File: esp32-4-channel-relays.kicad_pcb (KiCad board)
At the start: 2 copper layers, 86.4 x 86.6 mm, 63 parts, among them J1 Relay-1, J2 Relay-2, J3 Relay-3, J4 Relay-4, K1 SRD-05VDC-SL-C, K2 SRD-05VDC-SL-C, K3 SRD-05VDC-SL-C, K4 SRD-05VDC-SL-C, Q1 MBT3904DW1, Q2 BC547A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

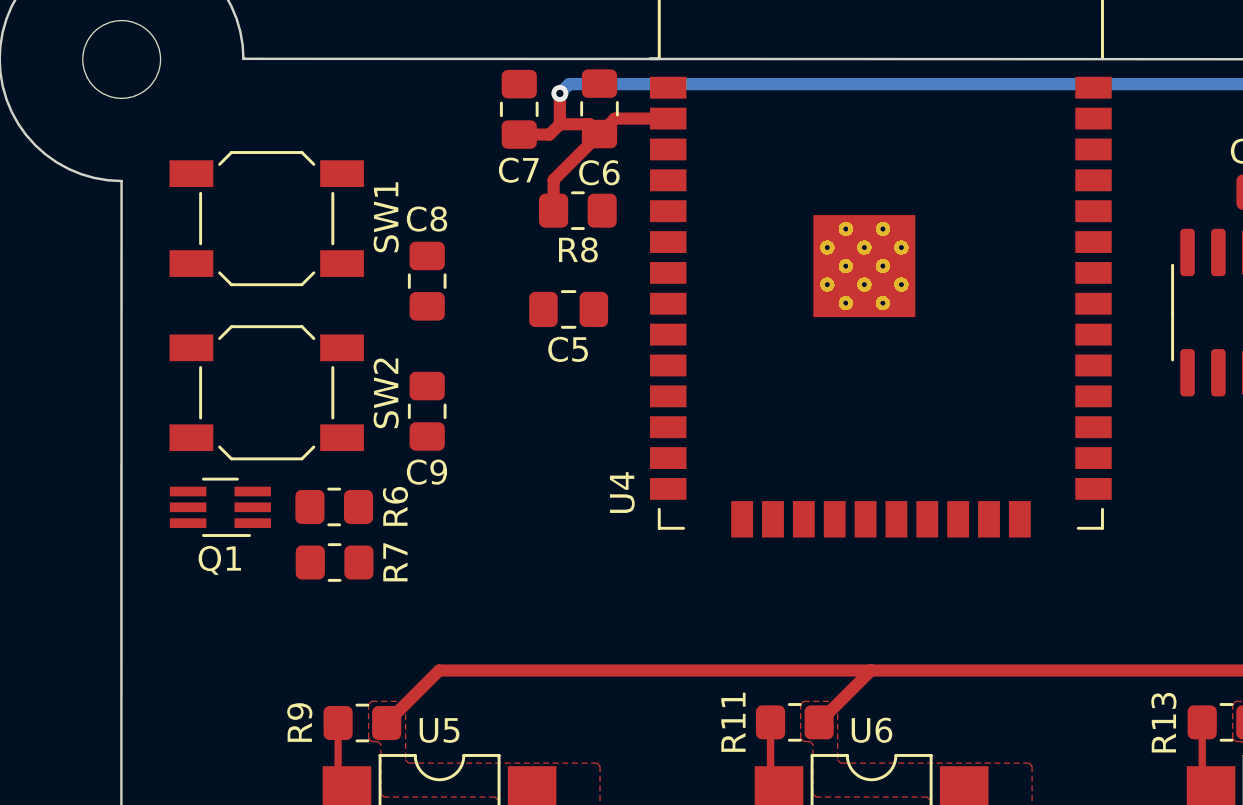
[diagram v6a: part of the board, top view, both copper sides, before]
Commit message: Routing Reset, Reset switch button and IO_0, IO_0 switch button
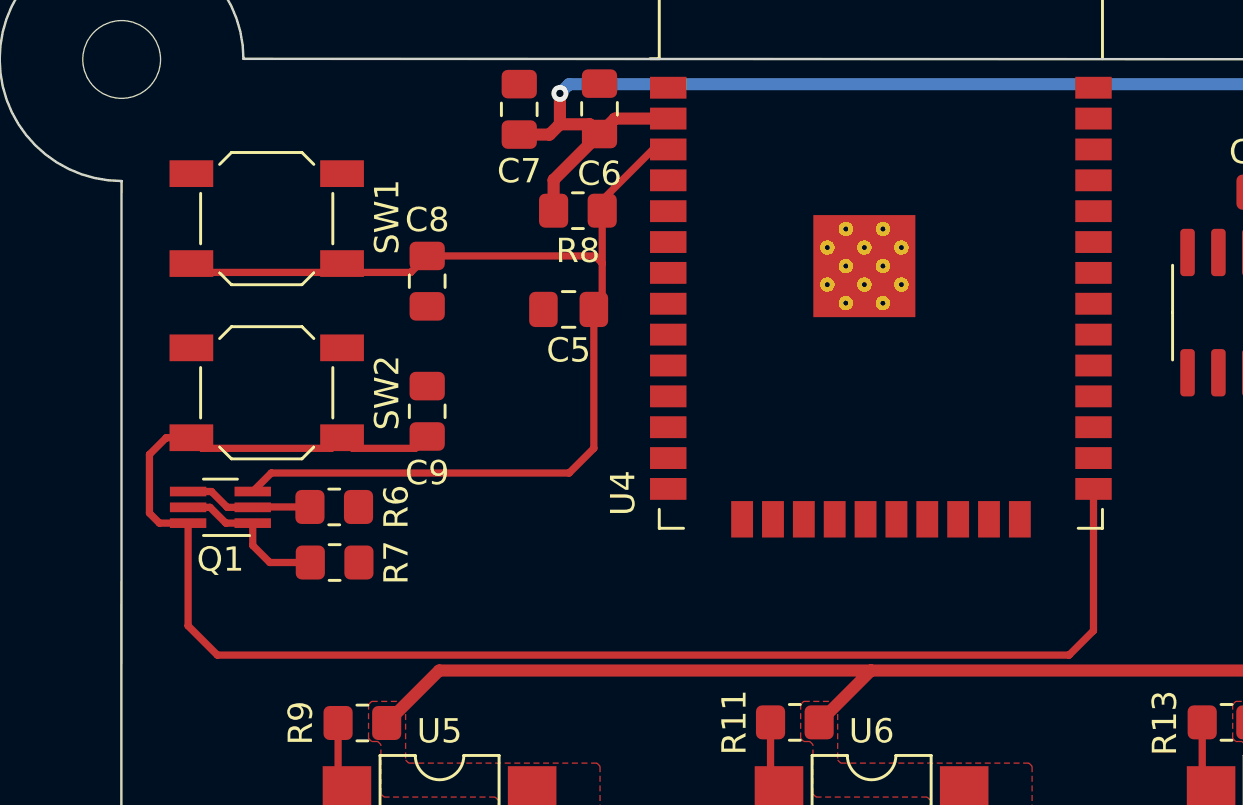
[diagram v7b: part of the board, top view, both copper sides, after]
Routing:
- net /IO_0: track 0.00 -> 64.9 mm
- net /RESET: track 0.00 -> 46.5 mm
- net Net-(Q1-B2): track 0.00 -> 6.51 mm
- net Net-(Q1-B1): track 0.00 -> 5.29 mm
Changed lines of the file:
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@@
   (segment (start 173.99 54.61) (end 145.034 54.61) (width 0.5) (layer "B.Cu") (net 3))
   (segment (start 175.387 57.531) (end 175.387 56.007) (width 0.5) (layer "B.Cu") (net 3))
+  (segment (start 129.488 61.993) (end 129.852 62.357) (width 0.3) (layer "F.Cu") (net 4))
+  (segment (start 135.688 61.993) (end 136.052 62.357) (width 0.3) (layer "F.Cu") (net 4))
+  (segment (start 146.3935 59.817) (end 146.3935 61.976) (width 0.3) (layer "F.Cu") (net 4))
+  (segment (start 132.775 70.612) (end 145.034 70.612) (width 0.3) (layer "F.Cu") (net 4))
+  (segment (start 146.0965 61.679) (end 146.3935 61.976) (width 0.3) (layer "F.Cu") (net 4))
+  (segment (start 146.3935 59.3845) (end 146.3935 59.817) (width 0.3) (layer "F.Cu") (net 4))
+  (segment (start 139.192 61.679) (end 146.0965 61.679) (width 0.3) (layer "F.Cu") (net 4))
+  (segment (start 132.013 71.374) (end 132.775 70.612) (width 0.3) (layer "F.Cu") (net 4))
+  (segment (start 148.481 57.297) (end 146.3935 59.3845) (width 0.3) (layer "F.Cu") (net 4))
+  (segment (start 146.05 69.596) (end 146.05 63.881) (width 0.3) (layer "F.Cu") (net 4))
+  (segment (start 136.052 62.357) (end 138.514 62.357) (width 0.3) (layer "F.Cu") (net 4))
+  (segment (start 129.852 62.357) (end 135.324 62.357) (width 0.3) (layer "F.Cu") (net 4))
+  (segment (start 145.034 70.612) (end 146.05 69.596) (width 0.3) (layer "F.Cu") (net 4))
+  (segment (start 146.3935 63.5375) (end 146.05 63.881) (width 0.3) (layer "F.Cu") (net 4))
+  (segment (start 146.3935 61.976) (end 146.3935 63.5375) (width 0.3) (layer "F.Cu") (net 4))
+  (segment (start 138.514 62.357) (end 139.192 61.679) (width 0.3) (layer "F.Cu") (net 4))
+  (segment (start 149.111 57.297) (end 148.481 57.297) (width 0.3) (layer "F.Cu") (net 4))
+  (segment (start 135.324 62.357) (end 135.688 61.993) (width 0.3) (layer "F.Cu") (net 4))
+  (segment (start 129.924 69.596) (end 135.252 69.596) (width 0.3) (layer "F.Cu") (net 5))
+  (segment (start 166.611 77.102) (end 166.611 71.267) (width 0.3) (layer "F.Cu") (net 5))
+  (segment (start 136.124 69.596) (end 138.7055 69.596) (width 0.3) (layer "F.Cu") (net 5))
+  (segment (start 128.452 69.16) (end 129.488 69.16) (width 0.3) (layer "F.Cu") (net 5))
+  (segment (start 129.353 76.902) (end 130.556 78.105) (width 0.3) (layer "F.Cu") (net 5))
+  (segment (start 127.762 69.85) (end 128.452 69.16) (width 0.3) (layer "F.Cu") (net 5))
+  (segment (start 135.252 69.596) (end 135.688 69.16) (width 0.3) (layer "F.Cu") (net 5))
+  (segment (start 129.353 72.674) (end 129.353 76.902) (width 0.3) (layer "F.Cu") (net 5))
+  (segment (start 130.556 78.105) (end 165.608 78.105) (width 0.3) (layer "F.Cu") (net 5))
+  (segment (start 127.762 72.263) (end 127.762 69.85) (width 0.3) (layer "F.Cu") (net 5))
+  (segment (start 135.688 69.16) (end 136.124 69.596) (width 0.3) (layer "F.Cu") (net 5))
+  (segment (start 129.353 72.674) (end 128.173 72.674) (width 0.3) (layer "F.Cu") (net 5))
+  (segment (start 129.488 69.16) (end 129.924 69.596) (width 0.3) (layer "F.Cu") (net 5))
+  (segment (start 138.7055 69.596) (end 139.192 69.1095) (width 0.3) (layer "F.Cu") (net 5))
+  (segment (start 165.608 78.105) (end 166.611 77.102) (width 0.3) (layer "F.Cu") (net 5))
+  (segment (start 128.173 72.674) (end 127.762 72.263) (width 0.3) (layer "F.Cu") (net 5))
   (segment (start 192.897 73.406) (end 195.063 73.406) (width 0.3) (layer "F.Cu") (net 6))
   (segment (start 135.89 86.106) (end 135.89 87.376) (width 0.3) (layer "F.Cu") (net 8))
@@
   (segment (start 191.516 66.421) (end 190.754 65.659) (width 0.5) (layer "B.Cu") (net 19))
   (segment (start 194.056 66.294) (end 194.183 66.421) (width 0.5) (layer "B.Cu") (net 19))
+  (segment (start 132.715 74.295) (end 132.013 73.593) (width 0.3) (layer "F.Cu") (net 32))
+  (segment (start 130.905894 72.674) (end 132.013 72.674) (width 0.3) (layer "F.Cu") (net 32))
+  (segment (start 132.013 73.593) (end 132.013 72.674) (width 0.3) (layer "F.Cu") (net 32))
+  (segment (start 130.255894 72.024) (end 130.905894 72.674) (width 0.3) (layer "F.Cu") (net 32))
+  (segment (start 129.353 72.024) (end 130.255894 72.024) (width 0.3) (layer "F.Cu") (net 32))
+  (segment (start 134.382 74.295) (end 132.715 74.295) (width 0.3) (layer "F.Cu") (net 32))
+  (segment (start 132.028 72.009) (end 132.013 72.024) (width 0.3) (layer "F.Cu") (net 33))
+  (segment (start 132.013 72.024) (end 130.963 72.024) (width 0.3) (layer "F.Cu") (net 33))
+  (segment (start 130.313 71.374) (end 129.353 71.374) (width 0.3) (layer "F.Cu") (net 33))
+  (segment (start 134.366 72.009) (end 132.028 72.009) (width 0.3) (layer "F.Cu") (net 33))
+  (segment (start 130.963 72.024) (end 130.313 71.374) (width 0.3) (layer "F.Cu") (net 33))
   (segment (start 133.736 90.424) (end 139.335 90.424) (width 0.3) (layer "F.Cu") (net 34))
   (segment (start 132.715 91.445) (end 133.736 90.424) (width 0.3) (layer "F.Cu") (net 34))

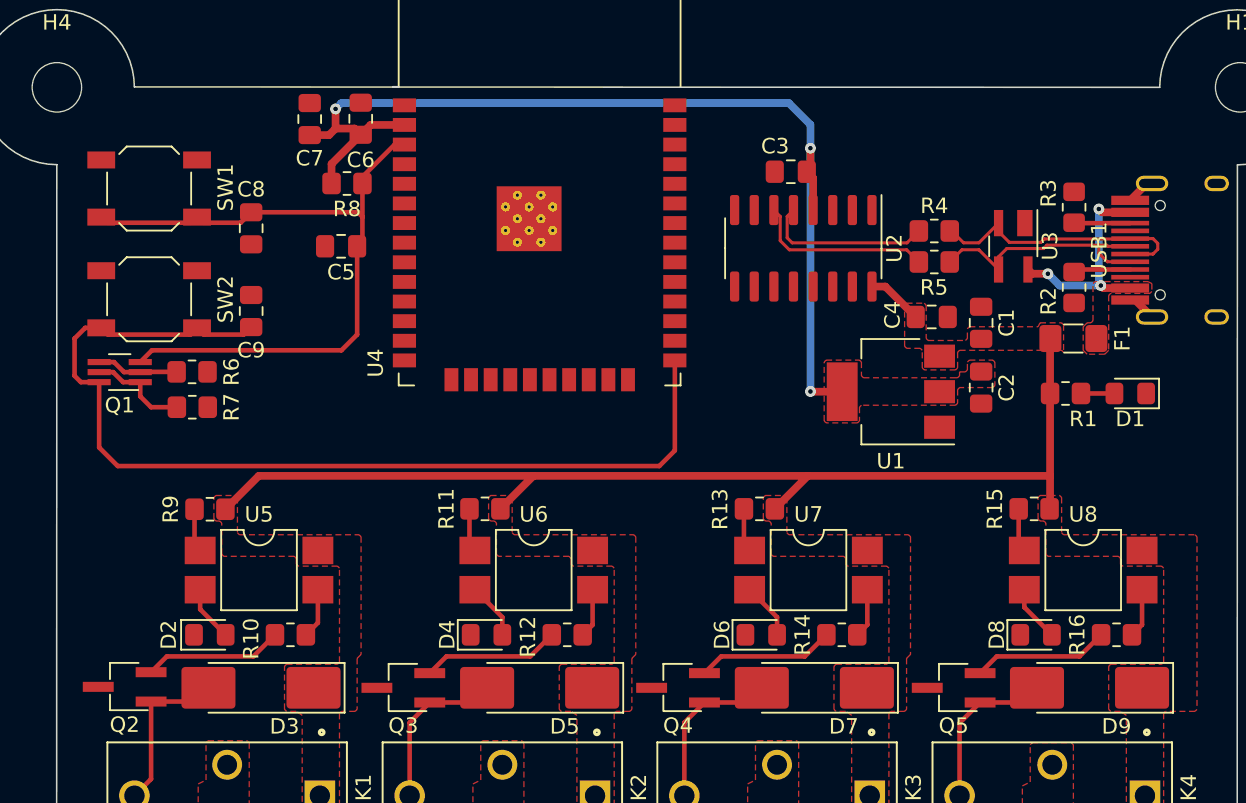
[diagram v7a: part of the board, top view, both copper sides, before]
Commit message: Routing GND, RTS and DTR
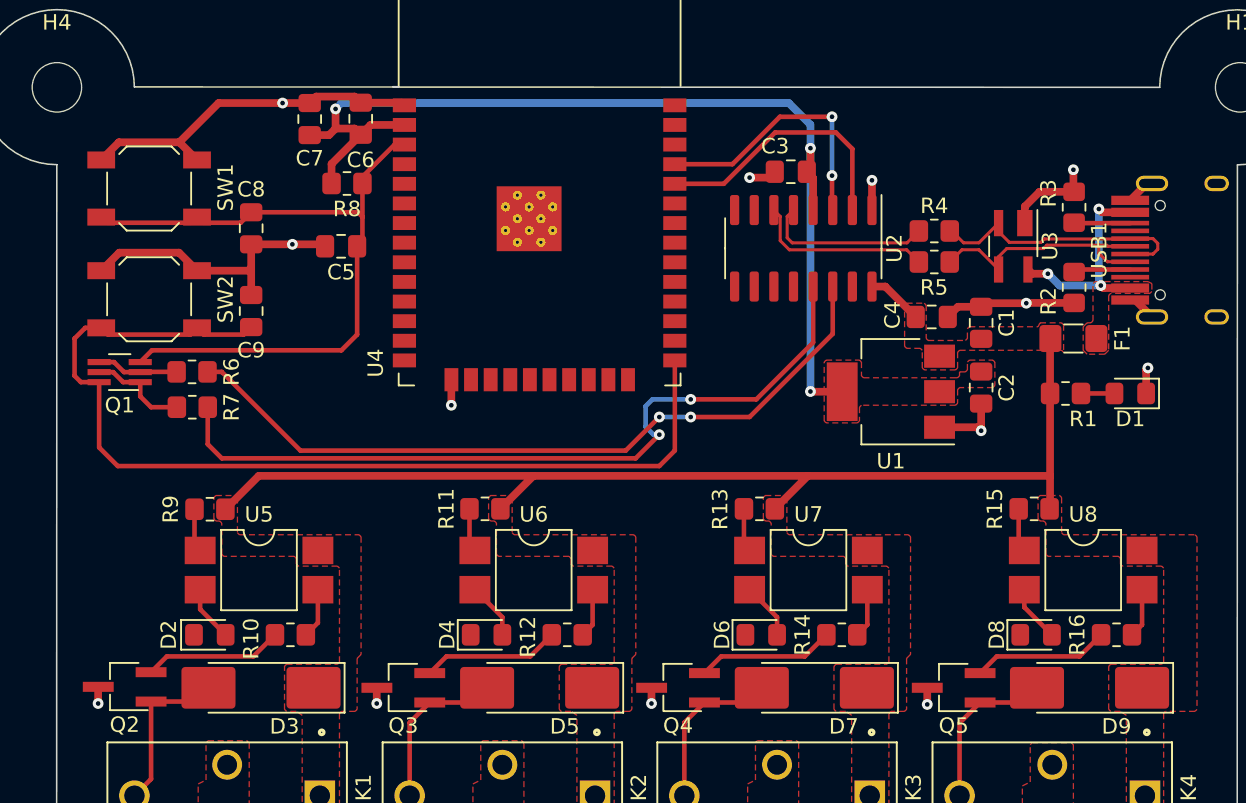
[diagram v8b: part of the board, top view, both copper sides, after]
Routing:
- net GND: track 3.74 -> 76.2 mm, vias 0 -> 13
- net /DTR: track 0.00 -> 51.2 mm, vias 0 -> 2
- net /RTS: track 0.00 -> 48.8 mm, vias 0 -> 2
- net /RX: track 0.00 -> 17.5 mm, vias 0 -> 2
- net /TX: track 0.00 -> 17.3 mm
